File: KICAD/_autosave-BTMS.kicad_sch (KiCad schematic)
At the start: 140 parts, among them J1 Batt_Ballance, J2 AUX_Charge, J3 Battery_IO, J4 Power_Out, J5 BTemp, J6 DSKY, J7 PWR_SW, J8 ICSP, J9 Heater, P1 USB_C_Plug, Q1 SSM3K341R, Q2 DMN65D8L, Q3 SSM3K341R, Q4 FDN340P, Q5 FDN340P, Q6 FDN340P, Q7 DMN65D8L, Q8 DMN65D8L, U1 ACS711xLCTR-25AB, U10 BA033CC0FP-E2, U11 AON7522E, U12 AON7522E, U13 LM62CIM3/NOPB, U14 FAN3100TSX, U15 FAN3100TSX, U16 AON7522E, U17 dsPIC30F3011-PT, U18 FT230XQ, U2 AP33771, U3 IS281-4, U4 Q294700DSGR, U5 SCF4030-12-0X, U6 AONR21321, U7 ACS711xLCTR-25AB, U8 IS281-4, U9 IRS2184

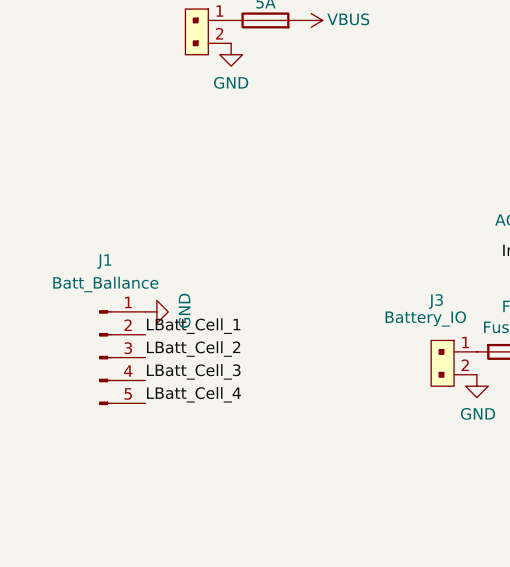
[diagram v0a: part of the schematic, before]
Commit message: Fixed 3.3v regulator not having correct pinout. Progressed board layout.
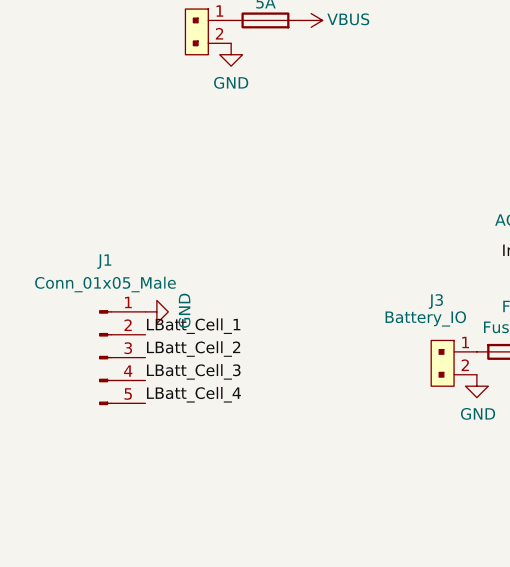
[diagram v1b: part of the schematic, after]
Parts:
- J1: value Batt_Ballance -> Conn_01x05_Male
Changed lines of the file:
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@@
     (in_bom yes) (on_board yes) (fields_autoplaced)
     (property "Reference" "J1" (id 0) (at 21.59 170.18 0))
-    (property "Value" "Batt_Ballance" (id 1) (at 21.59 172.72 0))
+    (property "Value" "Conn_01x05_Male" (id 1) (at 21.59 172.72 0))
     (property "Footprint" "Connector_JST:JST_VH_B5PS-VH_1x05_P3.96mm_Horizontal" (id 2) (at 20.955 180.975 0)
       (effects (font (size 1.27 1.27)) hide)
@@
     )
     (path "/17a7d292-9c5d-46fe-9cab-6f571fc5ef9a"
-      (reference "J1") (unit 1) (value "Batt_Ballance") (footprint "Connector_JST:JST_VH_B5PS-VH_1x05_P3.96mm_Horizontal")
+      (reference "J1") (unit 1) (value "Conn_01x05_Male") (footprint "Connector_JST:JST_VH_B5PS-VH_1x05_P3.96mm_Horizontal")
     )
     (path "/e3f15083-245b-4e47-a130-b04c1655b065"

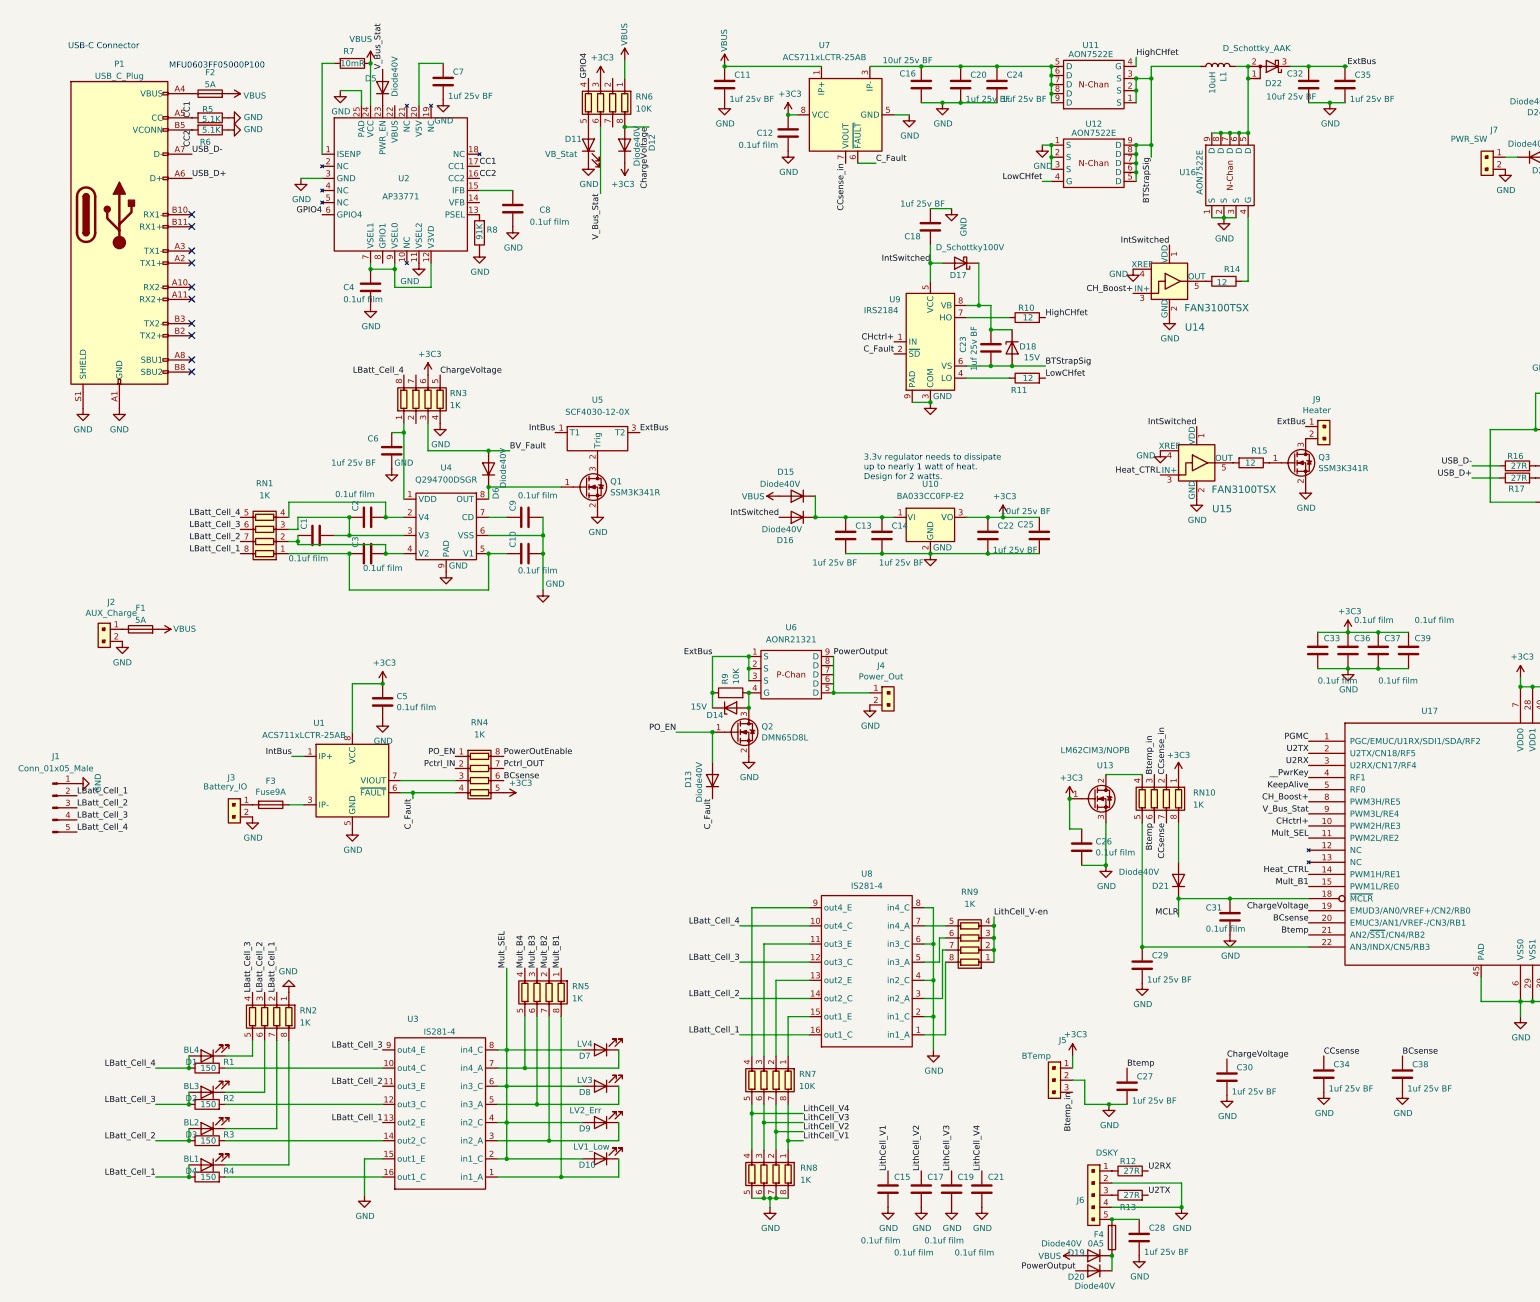
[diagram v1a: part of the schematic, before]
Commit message: Extended board and placed mounting points.
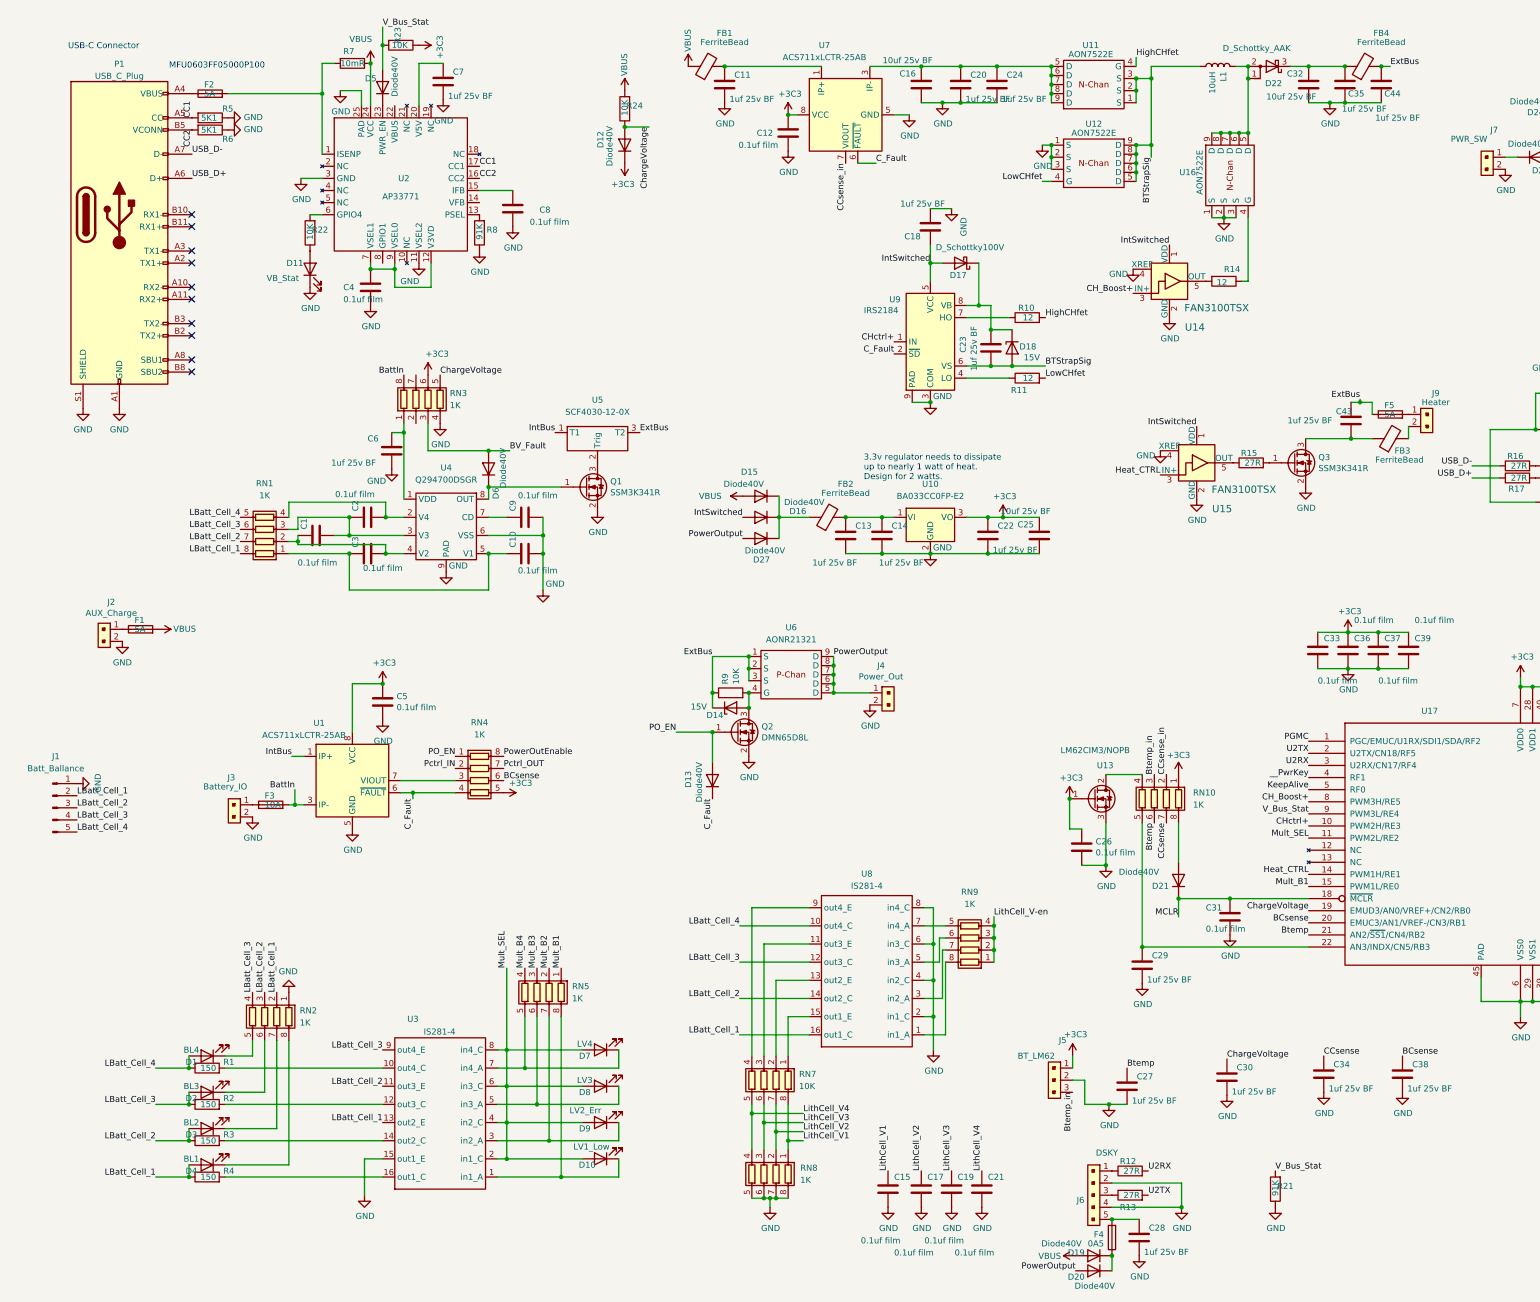
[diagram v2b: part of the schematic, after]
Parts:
- removed RN6: 10K, Resistor_SMD:R_Array_Convex_4x1206, symbol Device:R_Pack04
- added C43, C44: 1uf 25v BF, Capacitor_SMD:C_0603_1608Metric, symbol Device:C
- added D27: Diode40V, Diode_SMD:D_0603_1608Metric, symbol Device:D
- added F5: 5A, Fuse:Fuse_1206_3216Metric, symbol Device:Fuse
- added FB1, FB2, FB3, FB4: FerriteBead, Resistor_SMD:R_1206_3216Metric, symbol Device:FerriteBead
- added R21: 91K, Resistor_SMD:R_0603_1608Metric, symbol Device:R
- added R22, R23, R24: 10K, Resistor_SMD:R_0603_1608Metric, symbol Device:R
- F1, F2: footprint Fuse:Fuse_0603_1608Metric_Pad1.05x0.95mm_HandSolder -> Fuse:Fuse_1206_3216Metric; DK_Detail_Page (none) -> https://www.digikey.com/en/products/detail/bel-fuse-inc/C1F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; Digi-Key_PN (none) -> 507-1886-1-ND
- F3: value Fuse9A -> 10A; footprint Fuse:Fuse_0603_1608Metric_Pad1.05x0.95mm_HandSolder -> Fuse:Fuse_1206_3216Metric; DK_Detail_Page (none) -> https://www.digikey.com/en/products/detail/bel-fuse-inc/068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; Digi-Key_PN (none) -> 507-1942-1-ND
- F4: DK_Detail_Page (none) -> https://www.digikey.com/en/products/detail/bel-fuse-inc/C2Q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; Digi-Key_PN (none) -> 507-1089-1-ND
- J1: value Conn_01x05_Male -> Batt_Ballance
- J5: value BTemp -> BT_LM62
- R15: value 12 -> 27R; DK_Detail_Page https://www.digikey.com/en/products/detail/panasonic-electr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 -> https://www.digikey.com/en/products/detail/yageo/RC0603FR-1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; Digi-Key_PN 10-ERJ-UP3J120VCT-ND -> 13-RC0603FR-1327RLCT-ND
- R5, R6: value 5.1K -> 5K1; DK_Detail_Page (none) -> https://www.digikey.com/en/products/detail/yageo/RC0603FR-1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; Digi-Key_PN (none) -> 13-RC0603FR-135K1LCT-ND
- R7: footprint Resistor_SMD:R_0603_1608Metric -> Resistor_SMD:R_1206_3216Metric; DK_Detail_Page (none) -> https://www.digikey.com/en/products/detail/stackpole-electr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; Digi-Key_PN (none) -> CSR1206FT10L0CT-ND
- R8: DK_Detail_Page (none) -> https://www.digikey.com/en/products/detail/stackpole-electr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; Digi-Key_PN (none) -> RMCF0603FT91K0CT-ND
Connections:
- net +5C: now also R23.1
- net ChargeVoltage: now also R24.1
- net ExtBus: now also C43.1, C44.1, F5.1, FB4.2; no longer C32.1, C35.1, D22.3 (K), J9.1
- net GND: now also C44.2, R21.1
- net LBatt_Cell_4: no longer RN3.8 (R1.2)
- net PowerOutput: now also U6.6 (D), U6.7 (D), U6.8 (D), D27.2 (A)
- net VBUS: now also FB1.1, R24.2; no longer C11.1, F2.2, U7.1 (IP+), U7.2 (IP+)
- net V_Bus_Stat: now also R21.2, R23.2
- net at J9.2: now also FB3.2; no longer Q3.3 (D)
- net at U15.5 (OUT): now also R15.1; no longer R15.2
- net at C13.1, C14.1, U10.1 (VI): now also FB2.2; no longer D15.1 (K), D16.1 (K)
- net at J3.1: now also F3.1; no longer F3.2
- net BattIn: now reaches U1.3 (IP-), U1.4 (IP-)
- net BattIn: now also F3.2, RN3.8 (R1.2); no longer F3.1
- net at Q3.1 (G): now also R15.2; no longer R15.1
- net at R7.2, U2.1 (ISENP): now also F2.2
- net at D11.2 (A): now also R22.1
- net GPIO4: no longer names the net of U2.6 (GPIO4)
- net GPIO4: now also R22.2
- new net: C32.1, C35.1, D22.3 (K), FB4.1
- new net: C11.1, FB1.2, U7.1 (IP+), U7.2 (IP+)
- new net: D15.1 (K), D16.1 (K), D27.1 (K), FB2.1
- new net: F5.2, J9.1
- new net: C43.2, FB3.1, Q3.3 (D)
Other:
- moved on the sheet: D11, D15, D16, J9

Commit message: Added power switch button. Added credits and description silkscreening.
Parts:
- added SW1: PTS526, Button_Switch_SMD:SW_SPST_SKQG_WithStem, symbol Switch:SW_SPST
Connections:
- net GND: now also SW1.1 (A)
- net at D23.1 (K), J7.1: now also SW1.2 (B)
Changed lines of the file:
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@@
   (junction (at 194.945 120.015) (diameter 0) (color 0 0 0 0)
   )
+  (junction (at 325.755 44.45) (diameter 0) (color 0 0 0 0)
+  )
   (junction (at 161.925 25.4) (diameter 0) (color 0 0 0 0)
   )
@@
     (stroke (width 0) (type default) (color 0 0 0 0))
   )
+  (wire (pts (xy 325.755 34.925) (xy 325.755 44.45))
+    (stroke (width 0) (type default) (color 0 0 0 0))
+  )
   (wire (pts (xy 305.435 100.965) (xy 305.435 103.505))
     (stroke (width 0) (type default) (color 0 0 0 0))
@@
     (stroke (width 0) (type default) (color 0 0 0 0))
   )
+  (wire (pts (xy 325.12 34.925) (xy 325.755 34.925))
+    (stroke (width 0) (type default) (color 0 0 0 0))
+  )
   (wire (pts (xy 218.44 205.74) (xy 218.44 208.28))
     (stroke (width 0) (type default) (color 0 0 0 0))
@@
     (in_bom yes) (on_board yes)
     (property "Reference" "J7" (id 0) (at 323.4182 38.735 90))
-    (property "Value" "PWR_SW" (id 1) (at 318.135 40.64 90))
+    (property "Value" "PWR_SW" (id 1) (at 315.595 45.72 90))
     (property "Footprint" "Connector_PinHeader_2.54mm:PinHeader_1x02_P2.54mm_Vertical" (id 2) (at 328.295 49.53 0)
       (effects (font (size 1.524 1.524)) (justify left) hide)
@@
     (pin "2")
   )
+  (symbol (lib_id "Switch:SW_SPST") (at 320.04 34.925 0) (unit 1)
+    (in_bom yes) (on_board yes) (fields_autoplaced)
+    (property "Reference" "SW1" (id 0) (at 320.04 28.575 0))
+    (property "Value" "PTS526" (id 1) (at 320.04 31.115 0))
+    (property "Footprint" "Button_Switch_SMD:SW_SPST_SKQG_WithStem" (id 2) (at 320.04 34.925 0)
+      (effects (font (size 1.27 1.27)) hide)
+    )
+    (property "Datasheet" "~" (id 3) (at 320.04 34.925 0)
+      (effects (font (size 1.27 1.27)) hide)
+    )
+    (property "DK_Detail_Page" "https://www.digikey.com/en/products/detail/c-k/PTS526-SK15-SMTR2-LFS/10056626" (id 4) (at 320.04 34.925 0)
+      (effects (font (size 1.27 1.27)) hide)
+    )
+    (property "Digi-Key_PN" "CKN12221-1-ND" (id 5) (at 320.04 34.925 0)
+      (effects (font (size 1.27 1.27)) hide)
+    )
+    (pin "1")
+    (pin "2")
+  )
   (symbol (lib_id "Device:D_Schottky_AAK") (at 276.86 25.4 180) (unit 1)
     (in_bom yes) (on_board yes)
@@
     (pin "1")
   )
+  (symbol (lib_id "power:GND") (at 314.96 34.925 0) (unit 1)
+    (in_bom yes) (on_board yes)
+    (property "Reference" "#PWR0106" (id 0) (at 314.96 41.275 0)
+      (effects (font (size 1.27 1.27)) hide)
+    )
+    (property "Value" "GND" (id 1) (at 315.087 39.3192 0))
+    (property "Footprint" "" (id 2) (at 314.96 34.925 0)
+      (effects (font (size 1.27 1.27)) hide)
+    )
+    (property "Datasheet" "" (id 3) (at 314.96 34.925 0)
+      (effects (font (size 1.27 1.27)) hide)
+    )
+    (pin "1")
+  )
   (symbol (lib_id "Device:D") (at 159.385 175.26 90) (unit 1)
     (in_bom yes) (on_board yes)
@@
       (reference "#PWR0105") (unit 1) (value "GND") (footprint "")
     )
+    (path "/765cf6f4-9db5-4d66-8293-e4e2a047eae9"
+      (reference "#PWR0106") (unit 1) (value "GND") (footprint "")
+    )
     (path "/64c76206-53c0-4f04-b9c5-7beac0937b65"
       (reference "C1") (unit 1) (value "0.1uf film") (footprint "Capacitor_SMD:C_0603_1608Metric")
@@
       (reference "RN11") (unit 1) (value "10K") (footprint "Resistor_SMD:R_Array_Convex_4x1206")
     )
+    (path "/67647a8b-db66-4202-969a-7d17a16bd4a5"
+      (reference "SW1") (unit 1) (value "PTS526") (footprint "Button_Switch_SMD:SW_SPST_SKQG_WithStem")
+    )
     (path "/3202d53d-0910-47b2-a7db-5c708ae895e8"
